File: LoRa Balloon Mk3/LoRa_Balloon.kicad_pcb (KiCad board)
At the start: 2 copper layers, 30 x 47 mm, 245 parts, among them J1 Qwicc_6-pin, J2 Qwiic_4pin, U1 SKY67013-396LF_CID141, U2 SX1272IMLTRICT-ND_CID104, U3 SKY67013-396LF_CID141, U4 XCL205, U5 PE4259_CID105, U6 ATMEGA328P-MMH, X1 X1E0000210162_CID142, X2 7A-12.000MAAJ-T_CID117

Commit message: Created and added new component STEP files
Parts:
- removed the ? at (116.5, 104.0)
- removed the ? at (115.5, 104.0)
- removed the ? at (114.5, 104.0)
- removed the ? at (113.5, 104.0)
- removed the ? at (112.5, 104.0)
- removed the ? at (111.5, 104.0)
- removed the ? at (110.5, 104.0)
- removed the ? at (109.5, 104.0)
- removed the ? at (108.5, 104.0)
- removed the ? at (107.8, 104.7)
- removed the ? at (107.1, 105.4)
- removed the ? at (106.4, 106.1)
- removed the ? at (105.7, 106.8)
- removed the ? at (105.0, 107.6)
- removed the ? at (119.5, 104.0)
- removed the ? at (118.5, 104.0)
- removed the ? at (117.5, 104.0)
- removed J1: Qwicc_6-pin, dtusat:qwiic_6pin
- added ?: , dtusat:via-0.6mm-0.3mm_drill, F.Cu at (116.8, 109.5)
- added ?: , dtusat:via-0.6mm-0.3mm_drill, F.Cu at (113.0, 110.2)
- added ?: , dtusat:via-0.6mm-0.3mm_drill, F.Cu at (116.0, 110.2)
- added ?: , dtusat:via-0.6mm-0.3mm_drill, F.Cu at (115.2, 111.0)
- added ?: , dtusat:via-0.6mm-0.3mm_drill, F.Cu at (114.5, 111.7)
- added ?: , dtusat:via-0.6mm-0.3mm_drill, F.Cu at (113.7, 109.5)
- added ?: , dtusat:via-0.6mm-0.3mm_drill, F.Cu at (118.3, 104.9)
- added ?: , dtusat:via-0.6mm-0.3mm_drill, F.Cu at (119.1, 104.2)
- added ?: , dtusat:via-0.6mm-0.3mm_drill, F.Cu at (117.8, 102.2)
- added ?: , dtusat:via-0.6mm-0.3mm_drill, F.Cu at (117.0, 103.0)
- added ?: , dtusat:via-0.6mm-0.3mm_drill, F.Cu at (116.2, 103.8)
- added ?: , dtusat:via-0.6mm-0.3mm_drill, F.Cu at (115.5, 104.5)
- added ?: , dtusat:via-0.6mm-0.3mm_drill, F.Cu at (112.2, 111.0)
- added A2: GPS_ceramic_antenna, dtusat:Ceramic_Antenna, B.Cu at (105.9, 105.5)
- added U7: ublox_MAX-M8C, dtusat:ublox_MAX-M8C, B.Cu at (106.2, 120.8)
- J2: value Qwiic_4pin -> Edge_connector_9_pin; footprint dtusat:Qwiic_4-pin -> dtusat:Edge_connector_9_pin
- moved F1 13.8 mm to (116.0, 106.9), turned to 180 degrees
- moved J2 6.77 mm to (115.0, 142.5)
- moved A1 0.43 mm to (125.8, 102.8)
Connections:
- J2 pad 1: /RX -> GND
- J2 pad 2: /TX -> /Reset
- J2 pad 3: +3V3 -> /SCK
- J2 pad 4: GND -> /MISO
- U6 pad 15: Net-(U6-Pad15) -> /SCK
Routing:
- net /TX: track 21.6 -> 3.92 mm
- net Net-(A1-Pad1): track 23.4 -> 7.61 mm
- net /RX: track 12.2 -> 3.73 mm
- net GND: track 38.0 -> 31.3 mm, vias 22 -> 21
- net /RF_antenna: track 10.1 -> 5.65 mm
- net Net-(C26-Pad1): track 12.0 -> 9.85 mm
- net +3V3: track 100.3 -> 98.3 mm
- net /Reset: track 4.36 -> 2.51 mm
- net (no net): track 20.3 -> 22.1 mm, vias 4 -> 0
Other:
- outline, holes or cut-outs redrawn

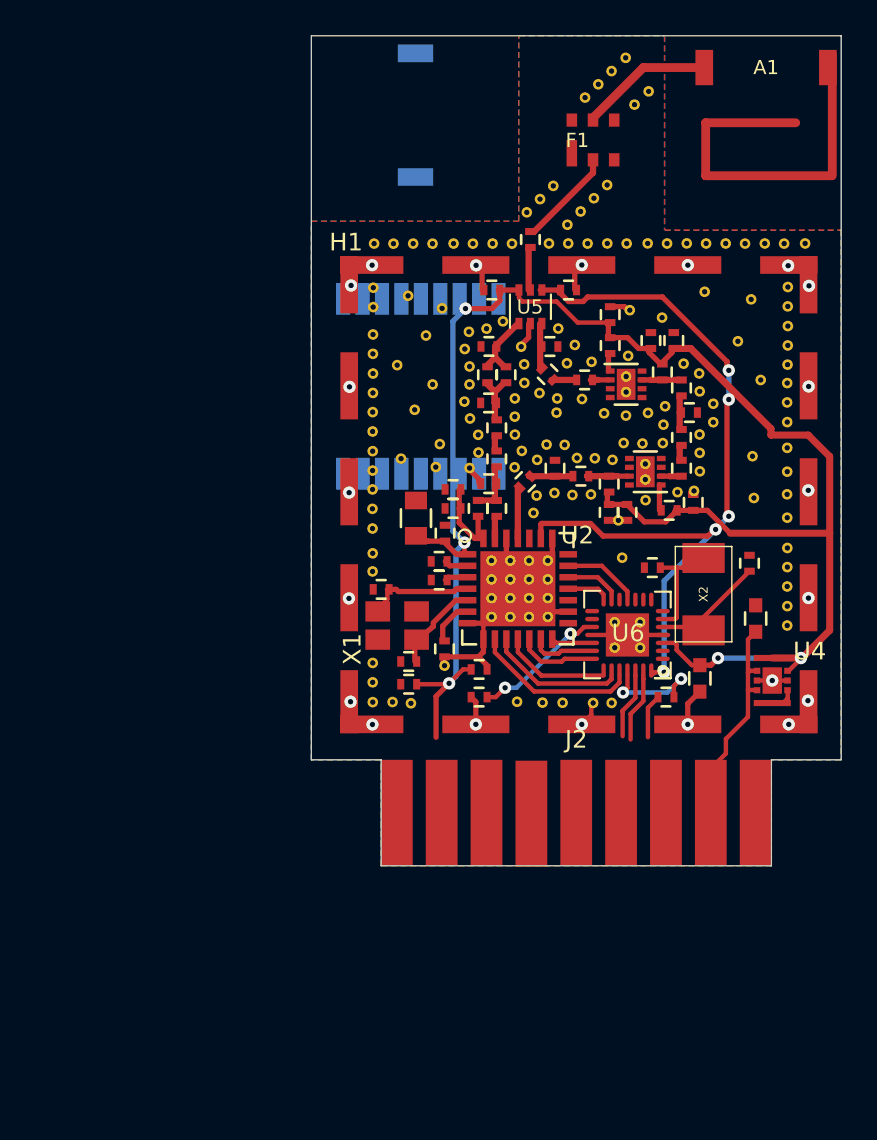
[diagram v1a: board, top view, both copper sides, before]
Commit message: Created and added new component STEP files
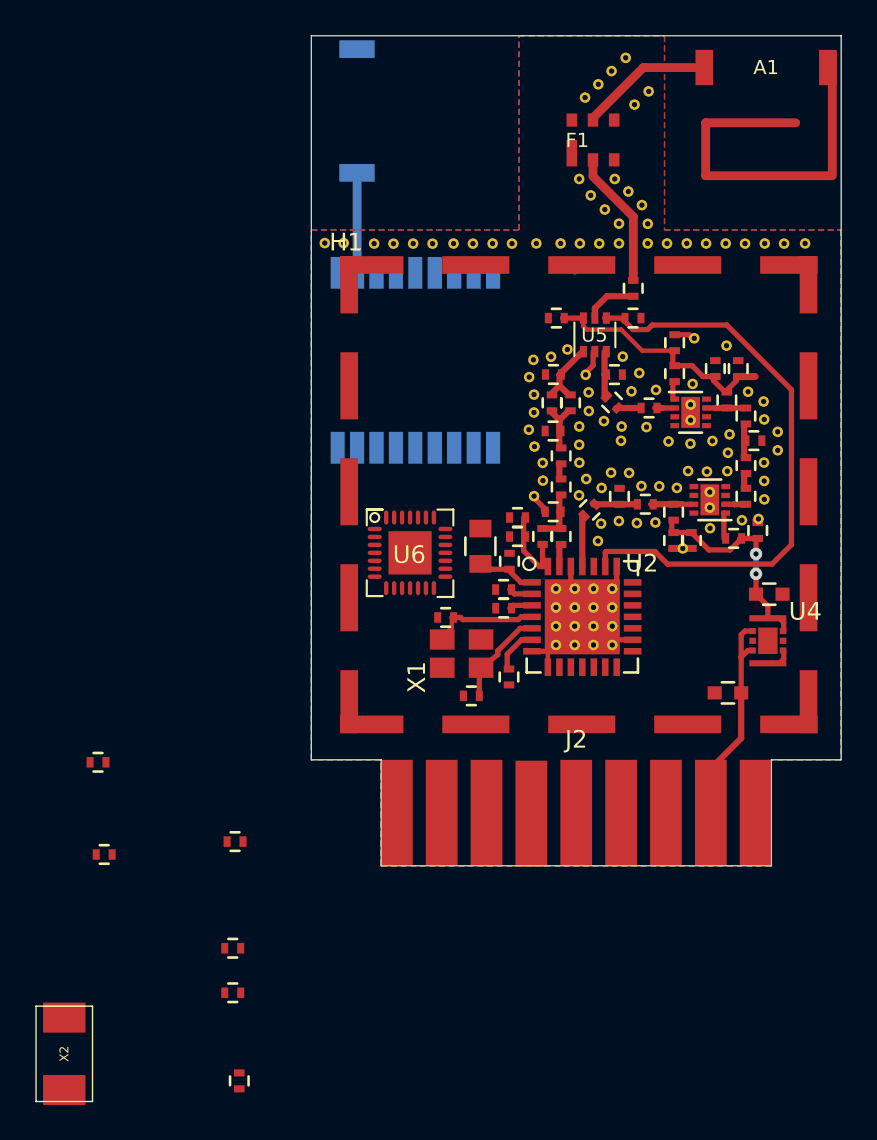
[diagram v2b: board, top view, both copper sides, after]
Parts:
- removed the ? at (116.8, 109.5)
- removed the ? at (113.0, 110.2)
- removed the ? at (113.5, 112.8)
- removed the ? at (111.3, 133.9)
- removed the ? at (110.2, 133.9)
- removed the ? at (111.3, 131.8)
- removed the ? at (110.2, 132.8)
- removed the ? at (116.0, 110.2)
- removed the ? at (110.2, 131.8)
- removed the ? at (111.3, 132.8)
- removed the ? at (112.3, 131.8)
- removed the ? at (112.3, 132.8)
- removed the ? at (112.3, 133.9)
- removed the ? at (113.4, 133.9)
- removed the ? at (113.4, 132.8)
- removed the ? at (113.4, 131.8)
- removed the ? at (113.4, 130.7)
- removed the ? at (112.3, 130.7)
- removed the ? at (115.2, 111.0)
- removed the ? at (111.3, 130.7)
- removed the ? at (110.2, 130.7)
- removed the ? at (112.6, 128.0)
- removed the ? at (112.8, 127.0)
- removed the ? at (113.8, 126.9)
- removed the ? at (114.8, 127.0)
- removed the ? at (115.8, 127.0)
- removed the ? at (118.9, 127.3)
- removed the ? at (120.7, 126.8)
- removed the ? at (121.7, 126.8)
- removed the ? at (122.0, 125.7)
- removed the ? at (122.0, 124.6)
- removed the ? at (122.0, 123.6)
- removed the ? at (122.8, 122.9)
- removed the ? at (122.8, 121.8)
- removed the ? at (122.0, 121.1)
- removed the ? at (122.0, 120.1)
- removed the ? at (117.9, 119.1)
- removed the ? at (114.9, 118.5)
- removed the ? at (114.0, 117.6)
- removed the ? at (117.6, 130.6)
- removed the ? at (115.9, 119.5)
- removed the ? at (114.5, 119.5)
- removed the ? at (112.9, 121.2)
- removed the ? at (113.9, 121.5)
- removed the ? at (113.9, 122.3)
- removed the ? at (115.3, 121.6)
- removed the ? at (116.6, 122.4)
- removed the ? at (117.8, 122.5)
- removed the ? at (119.1, 122.4)
- removed the ? at (121.1, 119.6)
- removed the ? at (118.6, 134.2)
- removed the ? at (120.0, 122.0)
- removed the ? at (119.9, 123.0)
- removed the ? at (119.9, 124.1)
- removed the ? at (118.8, 124.1)
- removed the ? at (117.7, 124.1)
- removed the ? at (117.1, 125.0)
- removed the ? at (116.1, 124.9)
- removed the ? at (115.0, 124.9)
- removed the ? at (114.3, 124.2)
- removed the ? at (113.3, 124.2)
- removed the ? at (117.2, 134.2)
- removed the ? at (111.9, 124.5)
- removed the ? at (112.8, 125.0)
- removed the ? at (111.5, 125.4)
- removed the ? at (111.5, 123.6)
- removed the ? at (111.5, 122.6)
- removed the ? at (111.5, 121.5)
- removed the ? at (112.1, 120.7)
- removed the ? at (112.1, 119.6)
- removed the ? at (111.9, 118.6)
- removed the ? at (109.0, 125.5)
- removed the ? at (118.6, 135.7)
- removed the ? at (109.5, 124.6)
- removed the ? at (109.4, 123.6)
- removed the ? at (109.0, 122.7)
- removed the ? at (108.7, 121.7)
- removed the ? at (109.0, 120.7)
- removed the ? at (109.0, 119.7)
- removed the ? at (108.7, 118.7)
- removed the ? at (108.9, 117.8)
- removed the ? at (109.9, 117.6)
- removed the ? at (110.8, 117.2)
- removed the ? at (117.2, 135.7)
- removed the ? at (105.6, 138.8)
- removed the ? at (113.7, 109.5)
- removed the ? at (117.4, 128.4)
- removed the ? at (118.0, 116.5)
- removed the ? at (119.9, 117.0)
- removed the ? at (107.5, 136.7)
- removed the ? at (118.9, 126.1)
- removed the ? at (118.9, 125.2)
- removed the ? at (117.8, 121.2)
- removed the ? at (117.8, 120.3)
- removed the ? at (122.3, 115.5)
- removed the ? at (124.9, 115.9)
- removed the ? at (124.2, 118.3)
- removed the ? at (125.4, 120.5)
- removed the ? at (125.0, 124.8)
- removed the ? at (125.1, 127.2)
- removed the ? at (107.0, 125.4)
- removed the ? at (105.1, 124.9)
- removed the ? at (104.9, 119.7)
- removed the ? at (106.9, 120.7)
- removed the ? at (107.4, 116.4)
- removed the ? at (107.3, 124.1)
- removed the ? at (106.5, 118.0)
- removed the ? at (105.9, 122.2)
- removed the ? at (105.5, 115.7)
- removed the ? at (114.2, 138.8)
- removed the ? at (116.0, 138.8)
- removed the ? at (117.0, 138.8)
- removed the ? at (111.7, 138.7)
- removed the ? at (113.1, 138.8)
- removed the ? at (127.0, 131.1)
- removed the ? at (126.9, 134.4)
- removed the ? at (127.0, 133.3)
- removed the ? at (126.9, 132.2)
- removed the ? at (127.0, 130.0)
- removed the ? at (126.9, 128.3)
- removed the ? at (126.9, 127.0)
- removed the ? at (117.9, 112.8)
- removed the ? at (116.8, 112.8)
- removed the ? at (114.5, 112.8)
- removed the ? at (115.6, 112.8)
- removed the ? at (126.9, 120.7)
- removed the ? at (126.9, 125.7)
- removed the ? at (126.9, 122.9)
- removed the ? at (126.9, 124.3)
- removed the ? at (126.9, 121.8)
- removed the ? at (127.0, 116.3)
- removed the ? at (127.0, 115.2)
- removed the ? at (127.0, 118.5)
- removed the ? at (127.0, 117.4)
- removed the ? at (127.0, 119.6)
- removed the ? at (104.6, 138.7)
- removed the ? at (103.5, 138.7)
- removed the ? at (103.5, 136.5)
- removed the ? at (103.5, 137.6)
- removed the ? at (103.5, 116.4)
- removed the ? at (103.5, 115.3)
- removed the ? at (103.5, 131.3)
- removed the ? at (103.5, 128.9)
- removed the ? at (103.5, 127.8)
- removed the ? at (103.5, 130.3)
- removed the ? at (103.5, 126.7)
- removed the ? at (103.5, 123.4)
- removed the ? at (112.2, 111.0)
- removed the ? at (103.5, 122.3)
- removed the ? at (103.5, 125.6)
- removed the ? at (103.5, 124.5)
- removed the ? at (103.5, 117.9)
- removed the ? at (103.5, 119.0)
- removed the ? at (103.5, 121.2)
- removed the ? at (103.5, 120.1)
- added ?: , dtusat:via-0.6mm-0.3mm_drill, F.Cu at (100.8, 112.7)
- added ?: , dtusat:via-0.6mm-0.3mm_drill, F.Cu at (112.7, 112.8)
- added ?: , dtusat:via-0.6mm-0.3mm_drill, F.Cu at (115.6, 126.1)
- added ?: , dtusat:via-0.6mm-0.3mm_drill, F.Cu at (116.4, 126.6)
- added ?: , dtusat:via-0.6mm-0.3mm_drill, F.Cu at (115.2, 127.0)
- added ?: , dtusat:via-0.6mm-0.3mm_drill, F.Cu at (115.2, 125.2)
- added ?: , dtusat:via-0.6mm-0.3mm_drill, F.Cu at (115.2, 124.2)
- added ?: , dtusat:via-0.6mm-0.3mm_drill, F.Cu at (115.2, 123.1)
- added ?: , dtusat:via-0.6mm-0.3mm_drill, F.Cu at (115.7, 122.2)
- added ?: , dtusat:via-0.6mm-0.3mm_drill, F.Cu at (115.7, 121.2)
- added ?: , dtusat:via-0.6mm-0.3mm_drill, F.Cu at (115.5, 120.2)
- added ?: , dtusat:via-0.6mm-0.3mm_drill, F.Cu at (112.6, 127.1)
- added ?: , dtusat:via-0.6mm-0.3mm_drill, F.Cu at (113.1, 126.2)
- added ?: , dtusat:via-0.6mm-0.3mm_drill, F.Cu at (113.1, 125.2)
- added ?: , dtusat:via-0.6mm-0.3mm_drill, F.Cu at (112.6, 124.3)
- added ?: , dtusat:via-0.6mm-0.3mm_drill, F.Cu at (112.3, 123.3)
- added ?: , dtusat:via-0.6mm-0.3mm_drill, F.Cu at (112.6, 122.3)
- added ?: , dtusat:via-0.6mm-0.3mm_drill, F.Cu at (112.6, 121.3)
- added ?: , dtusat:via-0.6mm-0.3mm_drill, F.Cu at (112.3, 120.3)
- added ?: , dtusat:via-0.6mm-0.3mm_drill, F.Cu at (112.6, 119.4)
- added ?: , dtusat:via-0.6mm-0.3mm_drill, F.Cu at (113.6, 119.2)
- added ?: , dtusat:via-0.6mm-0.3mm_drill, F.Cu at (114.5, 118.8)
- added ?: , dtusat:via-0.6mm-0.3mm_drill, F.Cu at (121.0, 130.0)
- added ?: , dtusat:via-0.6mm-0.3mm_drill, F.Cu at (121.7, 118.1)
- added ?: , dtusat:via-0.6mm-0.3mm_drill, F.Cu at (101.8, 112.7)
- added ?: , dtusat:via-0.6mm-0.3mm_drill, F.Cu at (123.5, 118.5)
- added ?: , dtusat:via-0.6mm-0.3mm_drill, F.Cu at (122.6, 127.7)
- added ?: , dtusat:via-0.6mm-0.3mm_drill, F.Cu at (122.6, 126.8)
- added ?: , dtusat:via-0.6mm-0.3mm_drill, F.Cu at (121.5, 122.8)
- added ?: , dtusat:via-0.6mm-0.3mm_drill, F.Cu at (121.5, 121.9)
- added ?: , dtusat:via-0.6mm-0.3mm_drill, F.Cu at (117.2, 109.1)
- added ?: , dtusat:via-0.6mm-0.3mm_drill, F.Cu at (117.4, 112.8)
- added ?: , dtusat:via-0.6mm-0.3mm_drill, F.Cu at (115.2, 112.8)
- added ?: , dtusat:via-0.6mm-0.3mm_drill, F.Cu at (116.3, 112.8)
- added ?: , dtusat:via-0.6mm-0.3mm_drill, F.Cu at (118.0, 109.8)
- added ?: , dtusat:via-0.6mm-0.3mm_drill, F.Cu at (114.1, 112.8)
- added ?: , dtusat:via-0.6mm-0.3mm_drill, F.Cu at (114.9, 135.5)
- added ?: , dtusat:via-0.6mm-0.3mm_drill, F.Cu at (113.9, 135.5)
- added ?: , dtusat:via-0.6mm-0.3mm_drill, F.Cu at (114.9, 133.4)
- added ?: , dtusat:via-0.6mm-0.3mm_drill, F.Cu at (113.9, 134.4)
- added ?: , dtusat:via-0.6mm-0.3mm_drill, F.Cu at (118.7, 110.6)
- added ?: , dtusat:via-0.6mm-0.3mm_drill, F.Cu at (113.9, 133.4)
- added ?: , dtusat:via-0.6mm-0.3mm_drill, F.Cu at (114.9, 134.4)
- added ?: , dtusat:via-0.6mm-0.3mm_drill, F.Cu at (116.0, 133.4)
- added ?: , dtusat:via-0.6mm-0.3mm_drill, F.Cu at (116.0, 134.4)
- added ?: , dtusat:via-0.6mm-0.3mm_drill, F.Cu at (116.0, 135.5)
- added ?: , dtusat:via-0.6mm-0.3mm_drill, F.Cu at (117.0, 135.5)
- added ?: , dtusat:via-0.6mm-0.3mm_drill, F.Cu at (117.0, 134.4)
- added ?: , dtusat:via-0.6mm-0.3mm_drill, F.Cu at (117.0, 133.4)
- added ?: , dtusat:via-0.6mm-0.3mm_drill, F.Cu at (117.0, 132.3)
- added ?: , dtusat:via-0.6mm-0.3mm_drill, F.Cu at (116.0, 132.3)
- added ?: , dtusat:via-0.6mm-0.3mm_drill, F.Cu at (119.0, 111.7)
- added ?: , dtusat:via-0.6mm-0.3mm_drill, F.Cu at (114.9, 132.3)
- added ?: , dtusat:via-0.6mm-0.3mm_drill, F.Cu at (113.9, 132.3)
- added ?: , dtusat:via-0.6mm-0.3mm_drill, F.Cu at (116.2, 129.6)
- added ?: , dtusat:via-0.6mm-0.3mm_drill, F.Cu at (116.4, 128.6)
- added ?: , dtusat:via-0.6mm-0.3mm_drill, F.Cu at (117.4, 128.5)
- added ?: , dtusat:via-0.6mm-0.3mm_drill, F.Cu at (118.4, 128.6)
- added ?: , dtusat:via-0.6mm-0.3mm_drill, F.Cu at (119.5, 128.6)
- added ?: , dtusat:via-0.6mm-0.3mm_drill, F.Cu at (122.6, 128.9)
- added ?: , dtusat:via-0.6mm-0.3mm_drill, F.Cu at (124.4, 128.4)
- added ?: , dtusat:via-0.6mm-0.3mm_drill, F.Cu at (125.3, 128.4)
- added ?: , dtusat:via-0.6mm-0.3mm_drill, F.Cu at (115.2, 109.1)
- added ?: , dtusat:via-0.6mm-0.3mm_drill, F.Cu at (125.6, 127.3)
- added ?: , dtusat:via-0.6mm-0.3mm_drill, F.Cu at (125.6, 126.2)
- added ?: , dtusat:via-0.6mm-0.3mm_drill, F.Cu at (125.6, 125.2)
- added ?: , dtusat:via-0.6mm-0.3mm_drill, F.Cu at (126.4, 124.5)
- added ?: , dtusat:via-0.6mm-0.3mm_drill, F.Cu at (126.4, 123.4)
- added ?: , dtusat:via-0.6mm-0.3mm_drill, F.Cu at (125.6, 122.7)
- added ?: , dtusat:via-0.6mm-0.3mm_drill, F.Cu at (125.6, 121.7)
- added ?: , dtusat:via-0.6mm-0.3mm_drill, F.Cu at (121.6, 120.7)
- added ?: , dtusat:via-0.6mm-0.3mm_drill, F.Cu at (118.6, 120.1)
- added ?: , dtusat:via-0.6mm-0.3mm_drill, F.Cu at (117.6, 119.2)
- added ?: , dtusat:via-0.6mm-0.3mm_drill, F.Cu at (115.8, 110.0)
- added ?: , dtusat:via-0.6mm-0.3mm_drill, F.Cu at (119.5, 121.1)
- added ?: , dtusat:via-0.6mm-0.3mm_drill, F.Cu at (118.1, 121.1)
- added ?: , dtusat:via-0.6mm-0.3mm_drill, F.Cu at (116.6, 122.8)
- added ?: , dtusat:via-0.6mm-0.3mm_drill, F.Cu at (117.6, 123.1)
- added ?: , dtusat:via-0.6mm-0.3mm_drill, F.Cu at (117.5, 123.9)
- added ?: , dtusat:via-0.6mm-0.3mm_drill, F.Cu at (119.0, 123.2)
- added ?: , dtusat:via-0.6mm-0.3mm_drill, F.Cu at (120.2, 124.0)
- added ?: , dtusat:via-0.6mm-0.3mm_drill, F.Cu at (121.5, 124.1)
- added ?: , dtusat:via-0.6mm-0.3mm_drill, F.Cu at (122.7, 123.9)
- added ?: , dtusat:via-0.6mm-0.3mm_drill, F.Cu at (124.7, 121.2)
- added ?: , dtusat:via-0.6mm-0.3mm_drill, F.Cu at (116.6, 110.8)
- added ?: , dtusat:via-0.6mm-0.3mm_drill, F.Cu at (123.7, 123.6)
- added ?: , dtusat:via-0.6mm-0.3mm_drill, F.Cu at (123.6, 124.6)
- added ?: , dtusat:via-0.6mm-0.3mm_drill, F.Cu at (123.6, 125.7)
- added ?: , dtusat:via-0.6mm-0.3mm_drill, F.Cu at (122.4, 125.7)
- added ?: , dtusat:via-0.6mm-0.3mm_drill, F.Cu at (121.3, 125.6)
- added ?: , dtusat:via-0.6mm-0.3mm_drill, F.Cu at (120.7, 126.6)
- added ?: , dtusat:via-0.6mm-0.3mm_drill, F.Cu at (119.7, 126.5)
- added ?: , dtusat:via-0.6mm-0.3mm_drill, F.Cu at (118.7, 126.5)
- added ?: , dtusat:via-0.6mm-0.3mm_drill, F.Cu at (118.0, 125.8)
- added ?: , dtusat:via-0.6mm-0.3mm_drill, F.Cu at (117.0, 125.7)
- moved X2 44.6 mm to (86.0, 158.7)
- moved C33 41.2 mm to (95.9, 160.2)
- moved C34 33.8 mm to (95.5, 155.2)
- moved C35 28.4 mm to (95.5, 152.7)
- moved C37 23.7 mm to (88.3, 147.4)
- moved C10 18.1 mm to (87.9, 142.1)
- moved C36 16.1 mm to (95.7, 146.6)
- moved U6 13.2 mm to (105.6, 130.3), turned to 0 degrees
- moved C32 6.45 mm to (118.2, 115.3)
- moved C31 6.18 mm to (125.9, 132.6), turned to 0 degrees
- moved C26 4.49 mm to (123.6, 138.2), turned to 180 degrees
- moved C18 4.05 mm to (109.1, 138.4)
- moved C11 3.98 mm to (122.9, 119.8)
- moved C12 3.98 mm to (124.2, 119.8)
- moved C21 3.98 mm to (121.5, 129.6)
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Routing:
- net +3V3: track 98.3 -> 30.0 mm, vias 5 -> 2
- net GND: track 31.3 -> 13.3 mm, vias 21 -> 0
- net /RXTX_SW: track 43.6 -> 33.4 mm, vias 5 -> 0
- net /DIO0: track 9.33 -> 0.00 mm
- net /DIO1: track 7.73 -> 0.00 mm
- net Net-(C33-Pad2): track 7.43 -> 0.00 mm
- net Net-(C36-Pad2): track 7.29 -> 0.00 mm, vias 2 -> 0
- net Net-(C34-Pad2): track 6.31 -> 0.00 mm
- net /DIO2: track 6.14 -> 0.00 mm
- net Net-(C35-Pad2): track 5.89 -> 0.00 mm, vias 2 -> 0
- net Net-(A2-Pad1): track 0.00 -> 5.71 mm
- net /DIO3: track 4.20 -> 0.00 mm
- net /RF_CS: track 4.12 -> 0.00 mm
- net /TX: track 3.92 -> 0.00 mm
- net /RX: track 3.73 -> 0.00 mm
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
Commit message: Finished board layout
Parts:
- removed the ? at (100.8, 112.7)
- removed the ? at (116.2, 129.6)
- added ?: , dtusat:via-0.6mm-0.3mm_drill, F.Cu at (118.5, 137.1)
- added ?: , dtusat:via-0.6mm-0.3mm_drill, F.Cu at (119.4, 116.1)
- added ?: , dtusat:via-0.6mm-0.3mm_drill, F.Cu at (119.4, 115.1)
- added ?: , dtusat:via-0.6mm-0.3mm_drill, F.Cu at (117.0, 115.1)
- added ?: , dtusat:via-0.6mm-0.3mm_drill, F.Cu at (116.0, 115.5)
- added ?: , dtusat:via-0.6mm-0.3mm_drill, F.Cu at (115.2, 116.0)
- added ?: , dtusat:via-0.6mm-0.3mm_drill, F.Cu at (114.2, 116.0)
- added ?: , dtusat:via-0.6mm-0.3mm_drill, F.Cu at (113.2, 116.0)
- added ?: , dtusat:via-0.6mm-0.3mm_drill, F.Cu at (112.4, 116.6)
- added ?: , dtusat:via-0.6mm-0.3mm_drill, F.Cu at (112.4, 117.6)
- added ?: , dtusat:via-0.6mm-0.3mm_drill, F.Cu at (106.2, 131.9)
- added ?: , dtusat:via-0.6mm-0.3mm_drill, F.Cu at (105.1, 126.0)
- added ?: , dtusat:via-0.6mm-0.3mm_drill, F.Cu at (104.8, 131.9)
- added ?: , dtusat:via-0.6mm-0.3mm_drill, F.Cu at (106.2, 130.5)
- added ?: , dtusat:via-0.6mm-0.3mm_drill, F.Cu at (104.8, 130.5)
- added ?: , dtusat:via-0.6mm-0.3mm_drill, F.Cu at (113.0, 112.7)
- added ?: , dtusat:via-0.6mm-0.3mm_drill, F.Cu at (123.4, 134.6)
- added ?: , dtusat:via-0.6mm-0.3mm_drill, F.Cu at (111.1, 125.7)
- added ?: , dtusat:via-0.6mm-0.3mm_drill, F.Cu at (123.6, 118.5)
- added ?: , dtusat:via-0.6mm-0.3mm_drill, F.Cu at (121.7, 119.0)
- added ?: , dtusat:via-0.6mm-0.3mm_drill, F.Cu at (119.4, 119.5)
- added ?: , dtusat:via-0.6mm-0.3mm_drill, F.Cu at (119.4, 118.2)
- added ?: , dtusat:via-0.6mm-0.3mm_drill, F.Cu at (120.2, 116.7)
- C33, C34, C36, C37, U6, X2: moved to B.Cu
- moved C10 35.6 mm to (123.0, 135.9), turned to 0 degrees
- moved X2 28.5 mm to (104.3, 136.9), turned to 0 degrees
- moved C37 25.7 mm to (104.0, 127.0)
- moved C36 24.2 mm to (110.0, 127.1), turned to 270 degrees
- moved C33 22.5 mm to (104.9, 139.5), turned to 90 degrees
- moved C35 18.2 mm to (107.2, 138.6)
- moved C34 17.6 mm to (103.6, 139.5), turned to 90 degrees
- moved C17 1.71 mm to (109.3, 133.6), turned to 270 degrees
- moved U6 0.94 mm to (105.5, 131.2)
- moved U7 0.94 mm to (106.8, 119.3)
- moved A2 0.94 mm to (103.5, 105.3)
- moved ? 0.90 mm to (122.6, 118.5)
- moved ? 0.84 mm to (111.9, 112.7)
- moved ? 0.80 mm to (102.8, 112.7)
- moved ? 0.56 mm to (110.8, 112.7)
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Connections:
- U4 pad GND: (no net) -> GND
- U6 pad 1: Net-(U6-Pad1) -> /GPS_RX
- U6 pad 2: Net-(U6-Pad2) -> /GPS_TX
- U6 pad 28: /RXTX_SW -> Net-(U6-Pad28)
- U6 pad 7: Net-(U6-Pad7) -> /RXTX_SW
- U7 pad 2: /RX -> /GPS_TX
- U7 pad 3: /TX -> /GPS_RX
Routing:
- net +3V3: track 30.0 -> 80.3 mm, vias 2 -> 5
- net /MOSI: track 0.00 -> 32.0 mm, vias 0 -> 2
- net /MISO: track 0.00 -> 31.2 mm, vias 0 -> 2
- net /SCK: track 0.00 -> 30.1 mm, vias 0 -> 2
- net /TX: track 0.00 -> 29.1 mm, vias 0 -> 2
- net /RX: track 0.00 -> 27.7 mm, vias 0 -> 2
- net GND: track 13.3 -> 34.7 mm, vias 0 -> 8
- net /RXTX_SW: track 33.4 -> 52.8 mm, vias 0 -> 1
- net /RF_CS: track 0.00 -> 19.2 mm, vias 0 -> 1
- net /GPS_TX: track 0.00 -> 15.6 mm, vias 0 -> 2
- net Net-(C33-Pad2): track 0.00 -> 15.3 mm, vias 0 -> 2
- net /DIO5: track 0.00 -> 14.9 mm, vias 0 -> 1
- net /DIO4: track 0.00 -> 14.0 mm, vias 0 -> 1
- net Net-(C34-Pad2): track 0.00 -> 13.9 mm, vias 0 -> 2
- net /DIO3: track 0.00 -> 13.2 mm, vias 0 -> 1
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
